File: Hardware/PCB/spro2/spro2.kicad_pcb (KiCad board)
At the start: 2 copper layers, 102.2 x 64 mm, 44 parts, among them J2 MAX30102, J3 Humidity sensor, U1 LM35-LP, U2 OPA340P, U3 TL074

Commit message: Second version of the PCB
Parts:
- moved U1 80.5 mm to (100.7, 84.0), turned to 0 degrees
- moved H3 4.59 mm to (172.2, 82.0)
- moved J2 4.37 mm to (140.0, 85.8)
- moved H1 4.00 mm to (77.8, 82.0)
- moved H4 2.25 mm to (172.2, 136.5)
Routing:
- net GND: track 250.1 -> 0.00 mm
- net /Temperature sensor filter and amplifier/Temp_In: track 9.55 -> 125.5 mm
- net +5V: track 137.3 -> 183.4 mm, vias 1 -> 0
- net +3.3V: track 54.3 -> 59.7 mm
- net Net-(A1-A5): track 37.8 -> 33.8 mm
- net Net-(A1-A4): track 42.9 -> 40.1 mm
- net /Humidity: track 77.4 -> 76.4 mm
- added copper zone on B.Cu, net GND
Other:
- board size 102.2 x 64 mm -> 100 x 60 mm

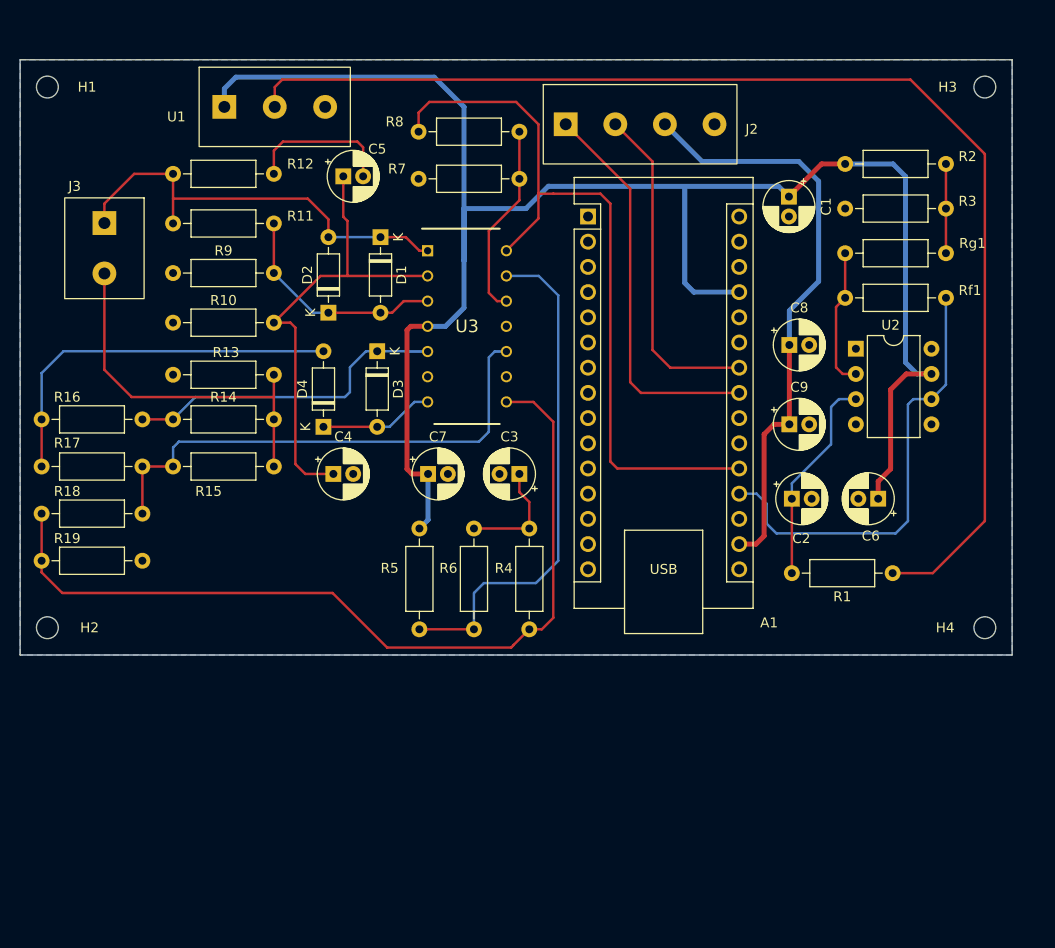
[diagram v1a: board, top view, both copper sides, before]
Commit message: Updated circuit
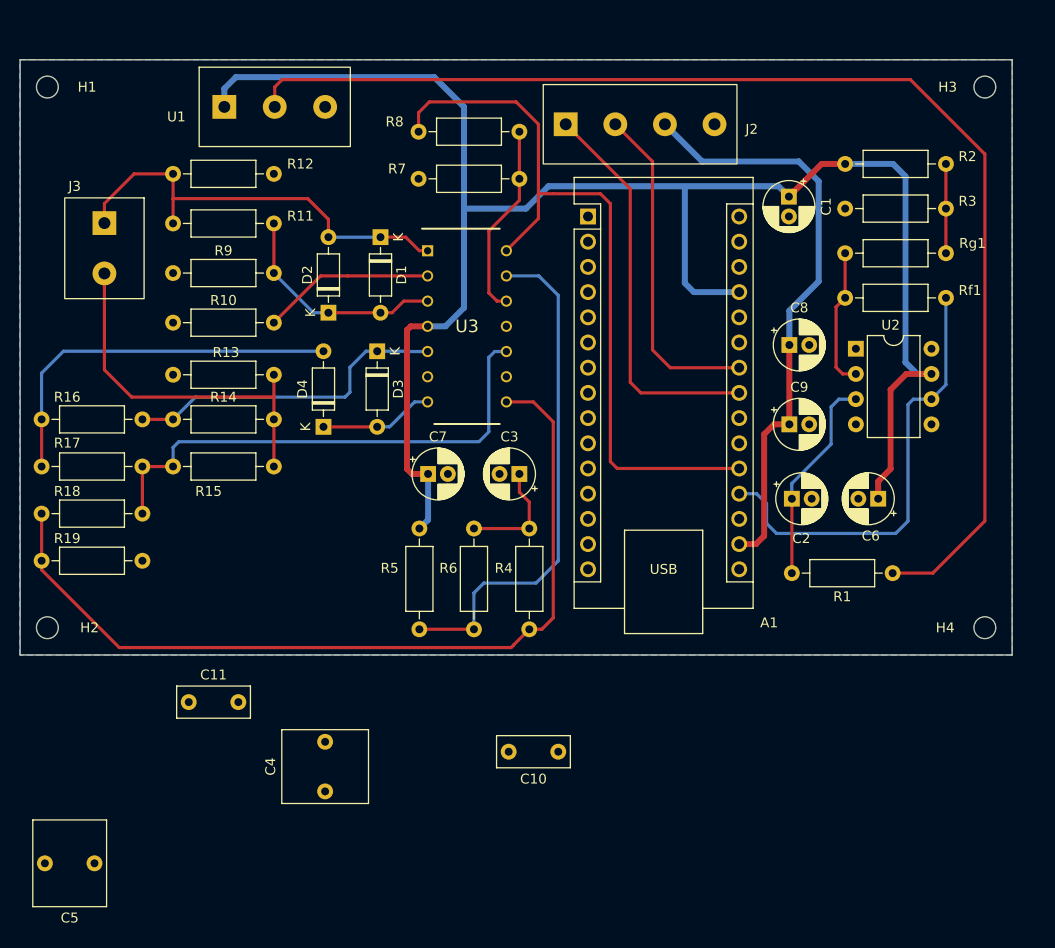
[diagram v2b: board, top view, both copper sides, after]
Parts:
- added C10: 100n, Capacitor_THT:C_Rect_L7.2mm_W3.0mm_P5.00mm_FKS2_FKP2_MKS2_MKP2, F.Cu at (129.2, 149.0)
- added C11: 100n, Capacitor_THT:C_Rect_L7.2mm_W3.0mm_P5.00mm_FKS2_FKP2_MKS2_MKP2, F.Cu at (92.0, 144.0)
- C4, C5: value 1590n -> 1.5u; footprint Capacitor_THT:CP_Radial_D5.0mm_P2.00mm -> Capacitor_THT:C_Rect_L7.2mm_W8.5mm_P5.00mm_FKP2_FKP2_MKS2_MKP2
- moved C5 73.7 mm to (82.5, 160.2), turned to 180 degrees
- moved C4 32.0 mm to (105.8, 153.0), turned to 90 degrees
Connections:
- C5 pad 1: Net-(U3A--) -> Net-(C11-Pad1)
- C5 pad 2: Net-(C5-Pad2) -> Net-(U3A--)
- R12 pad 1: Net-(C5-Pad2) -> Net-(C11-Pad1)
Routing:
- net Net-(U3A--): track 48.0 -> 17.5 mm
- net Net-(C5-Pad2): track 14.9 -> 0.00 mm

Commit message: Hopefully last version of PCB
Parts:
- removed J3: Humidity sensor, Diplomna:connector_2p
- added C12: 1.5u, Capacitor_THT:C_Rect_L13.0mm_W5.0mm_P10.00mm_FKS3_FKP3_MKS4, F.Cu at (112.0, 123.8)
- added C13: 100n, Capacitor_THT:C_Rect_L7.2mm_W2.5mm_P5.00mm_FKS2_FKP2_MKS2_MKP2, F.Cu at (110.5, 118.5)
- added J1: MAX30102, Diplomna:connector_4p, F.Cu at (147.5, 85.8)
- added R20: 200k, Resistor_THT:R_Axial_DIN0207_L6.3mm_D2.5mm_P10.16mm_Horizontal, F.Cu at (87.5, 136.0)
- added U4: ~, Package_DIP:DIP-8_W7.62mm, F.Cu at (127.8, 86.0)
- C1: value 4.7µF -> 100n; footprint Capacitor_THT:CP_Radial_D5.0mm_P2.00mm -> Capacitor_THT:C_Rect_L7.2mm_W2.5mm_P5.00mm_FKS2_FKP2_MKS2_MKP2
- C10: value 100n -> 1.5u; footprint Capacitor_THT:C_Rect_L7.2mm_W3.0mm_P5.00mm_FKS2_FKP2_MKS2_MKP2 -> Capacitor_THT:C_Rect_L13.0mm_W5.0mm_P10.00mm_FKS3_FKP3_MKS4
- C11: footprint Capacitor_THT:C_Rect_L7.2mm_W3.0mm_P5.00mm_FKS2_FKP2_MKS2_MKP2 -> Capacitor_THT:C_Rect_L7.2mm_W2.5mm_P5.00mm_FKS2_FKP2_MKS2_MKP2
- C2: value 2.2u -> 4.7µF
- C3: value 4.7u -> 100n; footprint Capacitor_THT:CP_Radial_D5.0mm_P2.00mm -> Capacitor_THT:C_Rect_L7.2mm_W2.5mm_P5.00mm_FKS2_FKP2_MKS2_MKP2
- C4: value 1.5u -> 100n; footprint Capacitor_THT:C_Rect_L7.2mm_W8.5mm_P5.00mm_FKP2_FKP2_MKS2_MKP2 -> Capacitor_THT:C_Rect_L7.2mm_W2.5mm_P5.00mm_FKS2_FKP2_MKS2_MKP2
- C5: value 1.5u -> 4.7µF; footprint Capacitor_THT:C_Rect_L7.2mm_W8.5mm_P5.00mm_FKP2_FKP2_MKS2_MKP2 -> Capacitor_THT:CP_Radial_D5.0mm_P2.00mm
- C6: value 100n -> 2.2u; footprint Capacitor_THT:CP_Radial_D5.0mm_P2.00mm -> Capacitor_THT:CP_Radial_D6.3mm_P2.50mm
- C7, C9: value 100n -> 100u; footprint Capacitor_THT:CP_Radial_D5.0mm_P2.00mm -> Capacitor_THT:CP_Radial_D10.0mm_P5.00mm
- C8: value 4.7µF -> 100u; footprint Capacitor_THT:CP_Radial_D5.0mm_P2.00mm -> Capacitor_THT:CP_Radial_D10.0mm_P5.00mm
- J2: value MAX30102 -> Humidity sensor; footprint Diplomna:connector_4p -> Diplomna:connector_2p
- R10: value 100 -> 43k
- R11: value 240 -> 100
- R13: value 47k -> 240
- R14: value 1k -> 100
- R15: value 1k -> 47k
- R16, R18: value 1k -> 200k
- R17: value 500 -> 200k
- R19: value 10k -> 100k
- R3: value 270 -> 240
- R4: value 3.3 -> 10k
- R5: value 91k -> 200
- R6: value 1k -> 22k
- R7: value 10k -> 91k
- R8: value 33k -> 1k
- R9: value 100 -> 10k
- moved C5 90.3 mm to (154.5, 105.8)
- moved J2 64.3 mm to (80.2, 109.5), turned to -90 degrees
- moved C4 63.4 mm to (93.5, 90.8), turned to -90 degrees
- moved R8 49.4 mm to (122.9, 135.8), turned to 90 degrees
- moved R6 45.6 mm to (110.7, 82.0), turned to 0 degrees
- moved C8 43.5 mm to (112.2, 91.5), turned to 90 degrees
- moved C3 41.2 mm to (166.5, 122.8)
- moved C9 33.0 mm to (122.1, 103.2)
- moved C10 31.1 mm to (102.0, 134.0), turned to 0 degrees
- moved C11 18.2 mm to (102.0, 128.8)
- moved R12 15.2 mm to (88.8, 100.2), turned to 0 degrees
- moved R11 14.4 mm to (88.8, 104.0), turned to 0 degrees
- moved C7 12.9 mm to (127.1, 114.2), turned to 180 degrees
- moved D4 12.8 mm to (94.2, 122.2), turned to -90 degrees
- moved R7 12.4 mm to (123.5, 82.0)
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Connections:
- C1 pad 1: +5V -> +3.3V
- C11 pad 1: Net-(C11-Pad1) -> Net-(U3A--)
- C11 pad 2: Net-(U3A--) -> GND
- C2 pad 1: Net-(U2-+) -> +3.3V
- C3 pad 1: Net-(C3-Pad1) -> +5V
- C4 pad 1: Net-(U3A--) -> +5V
- C5 pad 1: Net-(C11-Pad1) -> +5V
- C5 pad 2: Net-(U3A--) -> GND
- C6 pad 1: +5V -> Net-(U2-+)
- C7 pad 1: +5V -> Net-(C7-Pad1)
- C8 pad 1: +3.3V -> Net-(U4-CAP+)
- C8 pad 2: GND -> Net-(U4-CAP-)
- C9 pad 1: +3.3V -> -5V
- J2 pad 1: Net-(A1-A4) -> Net-(D1-K)
- J2 pad 2: Net-(A1-A5) -> Net-(J2-Pin_2)
- R10 pad 1: GND -> Net-(U3D-+)
- R10 pad 2: Net-(U3A--) -> /Humidity
- R11 pad 1: Net-(D1-A) -> GND
- R11 pad 2: Net-(D1-K) -> Net-(D1-A)
- R12 pad 1: Net-(C11-Pad1) -> GND
- R12 pad 2: Net-(D1-K) -> Net-(U3A--)
- R13 pad 1: Net-(J3-Pin_2) -> Net-(D1-A)
- R13 pad 2: GND -> Net-(D1-K)
- R14 pad 1: Net-(J3-Pin_2) -> Net-(C12-Pad1)
- R14 pad 2: Net-(D3-K) -> Net-(D1-K)
- R15 pad 1: Net-(J3-Pin_2) -> Net-(J2-Pin_2)
- R15 pad 2: Net-(U3C-+) -> GND
- R16 pad 1: Net-(D3-K) -> Net-(J2-Pin_2)
- R16 pad 2: Net-(D4-A) -> Net-(D3-K)
- R17 pad 1: Net-(D4-A) -> Net-(J2-Pin_2)
- R18 pad 1: Net-(U3C-+) -> Net-(D3-K)
- R18 pad 2: /Humidity Amplifier/Humidity_In -> Net-(D4-A)
- R19 pad 1: /Humidity Amplifier/Humidity_In -> Net-(D4-A)
- R19 pad 2: GND -> Net-(U3C-+)
- R4 pad 1: /Humidity Amplifier/Humidity_In -> /Temp
- R4 pad 2: Net-(C3-Pad1) -> Net-(R4-Pad2)
- R5 pad 1: +5V -> /Humidity Amplifier/Humidity_In
- R5 pad 2: Net-(U3D--) -> Net-(C7-Pad1)
- R6 pad 1: Net-(C3-Pad1) -> GND
- R6 pad 2: Net-(U3D--) -> Net-(R6-Pad2)
- R7 pad 1: GND -> Net-(R6-Pad2)
- R7 pad 2: Net-(U3D-+) -> Net-(U3D--)
- R8 pad 1: Net-(U3D-+) -> Net-(C7-Pad1)
- R8 pad 2: /Humidity -> Net-(U3D--)
- R9 pad 2: Net-(D1-A) -> Net-(U3D-+)
- Rf1 pad 2: /Temp -> Net-(R4-Pad2)
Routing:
- net Net-(R4-Pad2): track 0.00 -> 89.2 mm
- net /Humidity: track 76.4 -> 130.2 mm
- net /Humidity Amplifier/Humidity_In: track 87.1 -> 45.4 mm
- net Net-(U3D-+): track 19.6 -> 60.8 mm
- net Net-(J3-Pin_2): track 37.2 -> 0.00 mm
- net Net-(U3A--): track 17.5 -> 49.0 mm
- net Net-(C7-Pad1): track 0.00 -> 28.4 mm
- net Net-(J2-Pin_2): track 0.00 -> 26.7 mm
- net Net-(C12-Pad1): track 0.00 -> 18.2 mm
- net -5V: track 0.00 -> 17.4 mm
- net +5V: track 183.4 -> 166.1 mm
- net Net-(U4-CAP+): track 0.00 -> 16.7 mm
- net Net-(U3C-+): track 51.8 -> 67.2 mm
- net Net-(D4-A): track 38.7 -> 25.5 mm
- net Net-(D3-K): track 33.1 -> 45.7 mm
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
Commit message: pcb finalized
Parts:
- C2, C5: footprint Capacitor_THT:CP_Radial_D5.0mm_P2.00mm -> Capacitor_THT:CP_Radial_D7.5mm_P2.50mm
- moved C9 5.04 mm to (127.2, 103.2), turned to 180 degrees
- moved C6 1.30 mm to (155.2, 114.3)
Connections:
- C9 pad 1: -5V -> GND
- C9 pad 2: GND -> -5V
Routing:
- net Net-(U2-+): track 28.6 -> 27.5 mm

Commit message: Finished PCB
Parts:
- J1: footprint Diplomna:connector_4p -> SPRO_lib:connector_4p
- J2: footprint Diplomna:connector_2p -> SPRO_lib:connector_2p
- U1: footprint Diplomna:connector_3p -> SPRO_lib:connector_3p
